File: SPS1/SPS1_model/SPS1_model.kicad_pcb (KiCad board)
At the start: 4 copper layers, 133 x 93 mm, 5 parts, among them J1 TE_Eurocard_96pole

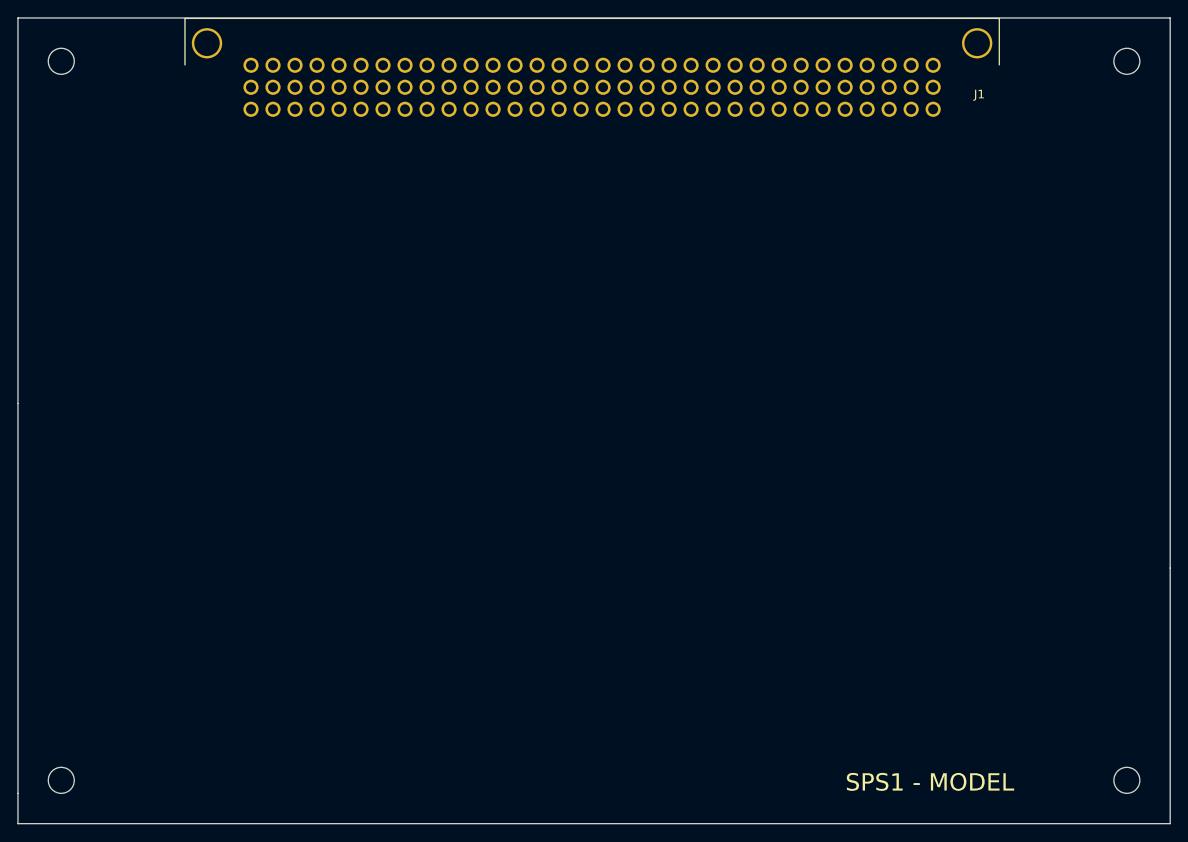
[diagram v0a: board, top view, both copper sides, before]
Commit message: Replacing old 3mm hole, cleaning
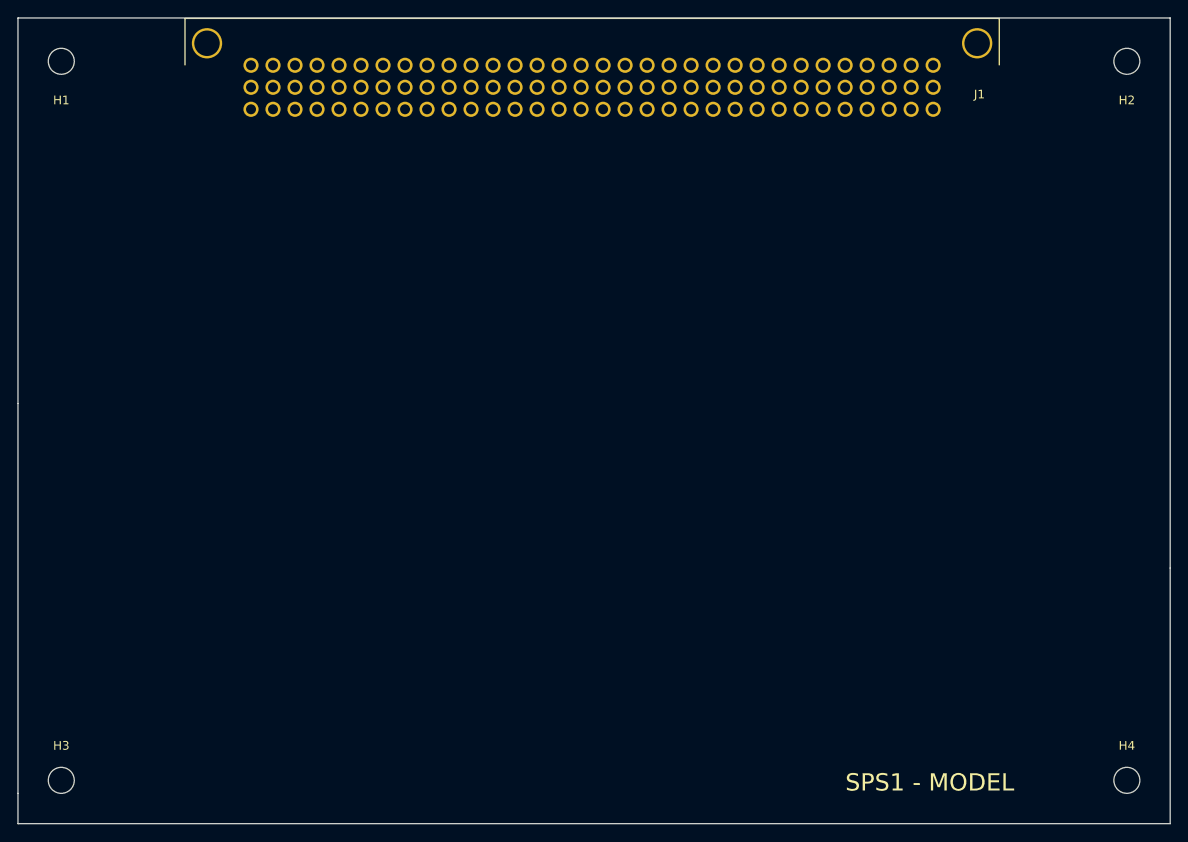
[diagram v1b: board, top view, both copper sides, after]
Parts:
- removed HOLE1, HOLE2, HOLE3, HOLE4: Hole_3mm, hole_3mm:Hole_3mm
- added H1: MountingHole_3mm, MountingHole:MountingHole_3mm, F.Cu at (66.0, 36.5)
- added H2: MountingHole_3mm, MountingHole:MountingHole_3mm, F.Cu at (189.0, 36.5)
- added H3: MountingHole_3mm, MountingHole:MountingHole_3mm, F.Cu at (66.0, 119.5)
- added H4: MountingHole_3mm, MountingHole:MountingHole_3mm, F.Cu at (189.0, 119.5)
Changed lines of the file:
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@@
-(kicad_pcb (version 20171130) (host pcbnew "(5.1.4)-1")
+(kicad_pcb (version 20171130) (host pcbnew "(5.1.6)-1")
   (general
     (thickness 1.6)
@@
   (title_block
     (title SPS1)
-    (date 2020-01-17)
-    (rev model)
-    (company "Guillaume Guillet")
+    (date 2020-07-01)
+    (rev "model rev2")
+    (company "Name here")
   )
   (layers
@@
     (pad_to_mask_clearance 0.2)
     (aux_axis_origin 61 31.5)
-    (visible_elements 7FFFF7FF)
+    (visible_elements 7FFFE7FF)
     (pcbplotparams
       (layerselection 0x010f0_ffffffff)
@@
     )
   )
-  (module hole_3mm:Hole_3mm locked (layer F.Cu)
+  (module MountingHole:MountingHole_3mm (layer F.Cu)
     (at 66 36.5)
-    (fp_text reference HOLE1 (at 1.8 3.4) (layer Eco2.User)
-      (effects (font (size 1 1) (thickness 0.15)))
-    )
-    (fp_text value Hole_3mm (at 4 -2.8) (layer F.Fab) hide
-      (effects (font (size 1 1) (thickness 0.15)))
-    )
-    (pad "" np_thru_hole circle (at 0 0) (size 3 3) (drill 3) (layers *.Cu *.Mask))
-  )
-  (module hole_3mm:Hole_3mm locked (layer F.Cu)
+    (descr "Mounting Hole 3mm, no annular")
+    (tags "mounting hole 3mm no annular")
+    (attr virtual)
+    (fp_text reference H1 (at 0 4.5) (layer F.SilkS)
+      (effects (font (size 1 1) (thickness 0.15)))
+    )
+    (fp_text value MountingHole_3mm (at 2.5 6) (layer F.Fab)
+      (effects (font (size 1 1) (thickness 0.15)))
+    )
+    (fp_circle (center 0 0) (end 3 0) (layer Cmts.User) (width 0.15))
+    (fp_circle (center 0 0) (end 3.25 0) (layer F.CrtYd) (width 0.05))
+    (fp_text user %R (at 0.3 0) (layer F.Fab)
+      (effects (font (size 1 1) (thickness 0.15)))
+    )
+    (pad 1 np_thru_hole circle (at 0 0) (size 3 3) (drill 3) (layers *.Cu *.Mask))
+  )
+  (module MountingHole:MountingHole_3mm (layer F.Cu)
     (at 189 36.5)
-    (fp_text reference HOLE2 (at 1.8 3.4) (layer Eco2.User)
-      (effects (font (size 1 1) (thickness 0.15)))
-    )
-    (fp_text value Hole_3mm (at 1 -2.8) (layer F.Fab) hide
-      (effects (font (size 1 1) (thickness 0.15)))
-    )
-    (pad "" np_thru_hole circle (at 0 0) (size 3 3) (drill 3) (layers *.Cu *.Mask))
-  )
-  (module hole_3mm:Hole_3mm locked (layer F.Cu)
+    (descr "Mounting Hole 3mm, no annular")
+    (tags "mounting hole 3mm no annular")
+    (attr virtual)
+    (fp_text reference H2 (at 0 4.5) (layer F.SilkS)
+      (effects (font (size 1 1) (thickness 0.15)))
+    )
+    (fp_text value MountingHole_3mm (at -2.5 6) (layer F.Fab)
+      (effects (font (size 1 1) (thickness 0.15)))
+    )
+    (fp_circle (center 0 0) (end 3 0) (layer Cmts.User) (width 0.15))
+    (fp_circle (center 0 0) (end 3.25 0) (layer F.CrtYd) (width 0.05))
+    (fp_text user %R (at 0.3 0) (layer F.Fab)
+      (effects (font (size 1 1) (thickness 0.15)))
+    )
+    (pad 1 np_thru_hole circle (at 0 0) (size 3 3) (drill 3) (layers *.Cu *.Mask))
+  )
+  (module MountingHole:MountingHole_3mm (layer F.Cu)
+    (at 66 119.5)
+    (descr "Mounting Hole 3mm, no annular")
+    (tags "mounting hole 3mm no annular")
+    (attr virtual)
+    (fp_text reference H3 (at 0 -4) (layer F.SilkS)
+      (effects (font (size 1 1) (thickness 0.15)))
+    )
+    (fp_text value MountingHole_3mm (at 8 4) (layer F.Fab)
+      (effects (font (size 1 1) (thickness 0.15)))
+    )
+    (fp_circle (center 0 0) (end 3.25 0) (layer F.CrtYd) (width 0.05))
+    (fp_circle (center 0 0) (end 3 0) (layer Cmts.User) (width 0.15))
+    (fp_text user %R (at 0.3 0) (layer F.Fab)
+      (effects (font (size 1 1) (thickness 0.15)))
+    )
+    (pad 1 np_thru_hole circle (at 0 0) (size 3 3) (drill 3) (layers *.Cu *.Mask))
+  )
+  (module MountingHole:MountingHole_3mm (layer F.Cu)
     (at 189 119.5)
-    (fp_text reference HOLE3 (at -3.5 3) (layer Eco2.User)
-      (effects (font (size 1 1) (thickness 0.15)))
-    )
-    (fp_text value Hole_3mm (at 1 -2.8) (layer F.Fab) hide
-      (effects (font (size 1 1) (thickness 0.15)))
-    )
-    (pad "" np_thru_hole circle (at 0 0) (size 3 3) (drill 3) (layers *.Cu *.Mask))
-  )
-  (module hole_3mm:Hole_3mm locked (layer F.Cu)
-    (at 66 119.5)
-    (fp_text reference HOLE4 (at 3 2.5) (layer Eco2.User)
-      (effects (font (size 1 1) (thickness 0.15)))
-    )
-    (fp_text value Hole_3mm (at 2.5 -2.8) (layer F.Fab) hide
-      (effects (font (size 1 1) (thickness 0.15)))
-    )
-    (pad "" np_thru_hole circle (at 0 0) (size 3 3) (drill 3) (layers *.Cu *.Mask))
+    (descr "Mounting Hole 3mm, no annular")
+    (tags "mounting hole 3mm no annular")
+    (attr virtual)
+    (fp_text reference H4 (at 0 -4) (layer F.SilkS)
+      (effects (font (size 1 1) (thickness 0.15)))
+    )
+    (fp_text value MountingHole_3mm (at -8 4) (layer F.Fab)
+      (effects (font (size 1 1) (thickness 0.15)))
+    )
+    (fp_circle (center 0 0) (end 3.25 0) (layer F.CrtYd) (width 0.05))
+    (fp_circle (center 0 0) (end 3 0) (layer Cmts.User) (width 0.15))
+    (fp_text user %R (at 0.3 0) (layer F.Fab)
+      (effects (font (size 1 1) (thickness 0.15)))
+    )
+    (pad 1 np_thru_hole circle (at 0 0) (size 3 3) (drill 3) (layers *.Cu *.Mask))
   )
   (dimension 2.85 (width 0.15) (layer Eco2.User)
